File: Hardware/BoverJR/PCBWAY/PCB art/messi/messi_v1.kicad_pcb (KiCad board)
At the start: 2 copper layers, 35 x 35 mm, 3 parts

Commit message: agregue a maradoooooooooo
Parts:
- added H4: Mounting_Hole, EESTN5:maradov1_bcu, F.Cu at (139.8, 98.1)
- H3: footprint EESTN5:bover_nombre2 -> EESTN5:bover_nombre

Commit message: terrmine llavero messi
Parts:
- added H5: Mounting_Hole, EESTN5:afa_mm, F.Cu at (126.2, 91.8)
- added H6: Mounting_Hole, EESTN5:bover_mm, F.Cu at (153.2, 93.4)
- H2: footprint EESTN5:logo_messiv3 -> EESTN5:messi
- moved H3 27.6 mm to (128.4, 86.2), turned to 45 degrees
- moved H1 1.80 mm to (140.0, 79.2)
- moved H2 1.43 mm to (136.0, 91.1)
- moved H4 0.36 mm to (139.6, 97.8)
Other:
- board size 35 x 35 mm -> 40 x 40 mm

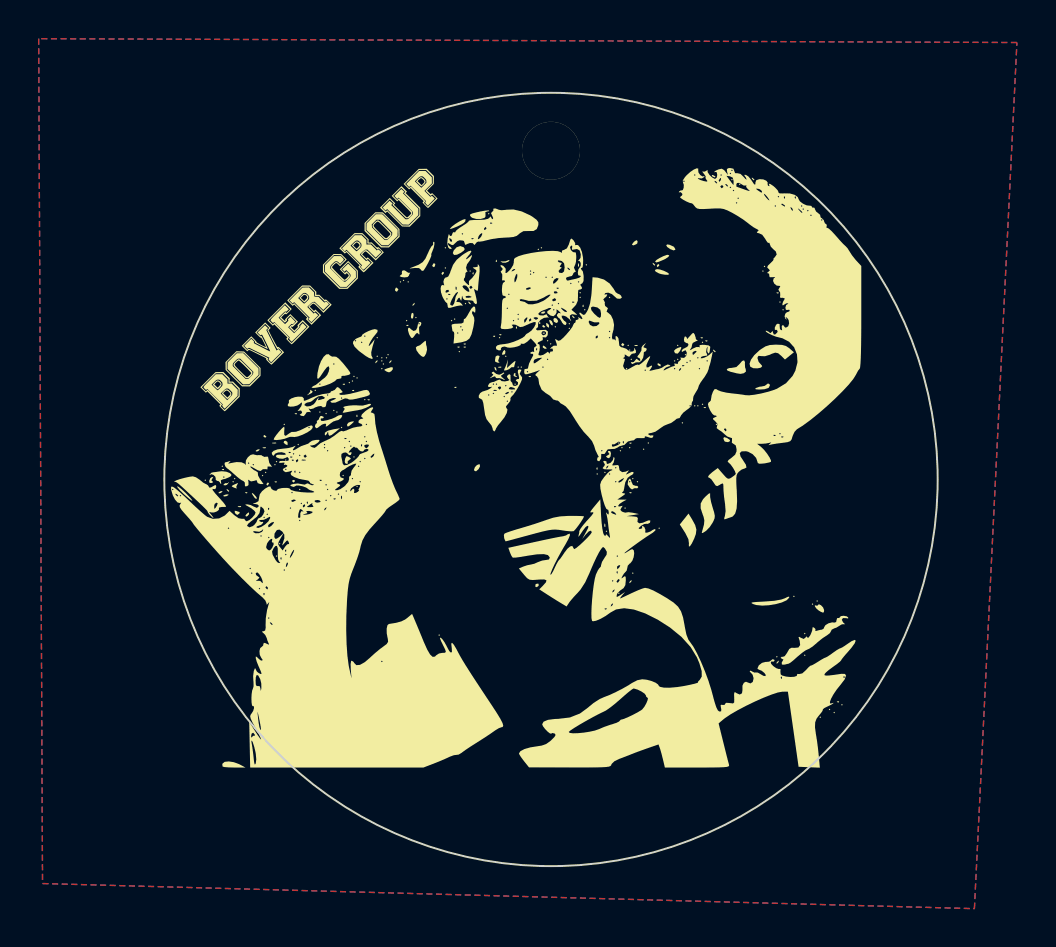
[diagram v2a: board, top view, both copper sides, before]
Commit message: esperando verificacion de pcbway ya cargue 6 gerber
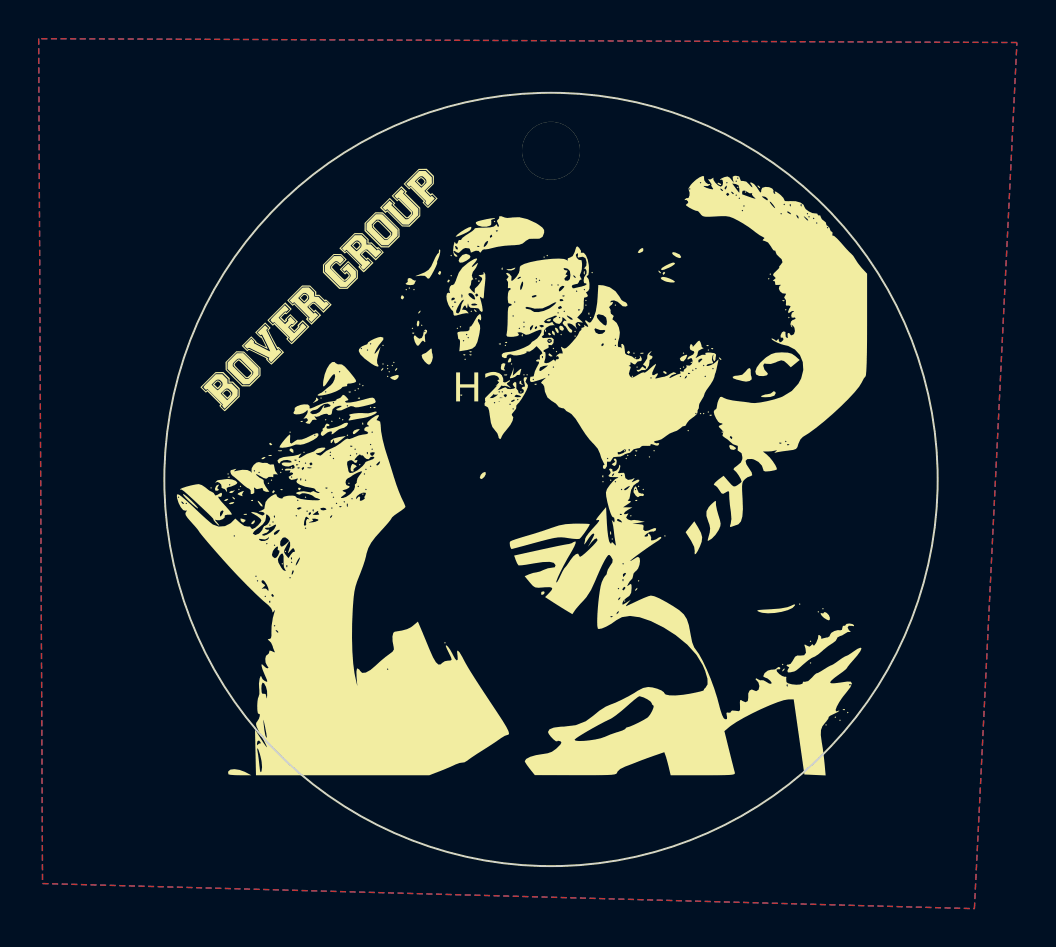
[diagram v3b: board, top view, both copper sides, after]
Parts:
- moved H4 0.63 mm to (139.0, 98.0)
- moved H2 0.50 mm to (136.3, 91.5)
